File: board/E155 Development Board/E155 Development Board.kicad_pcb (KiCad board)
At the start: 2 copper layers, 106.9 x 105.3 mm, 48 parts, among them J1 Screw_Terminal_01x02, J2 Conn_01x03, J3 Conn_01x02, J4 Conn_01x02, J6 Conn_02x20_Odd_Even, J7 Conn_01x06, SW0 SW_Push, SW1 SW_Push, SW2 SW_Push, SW3 SW_Push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

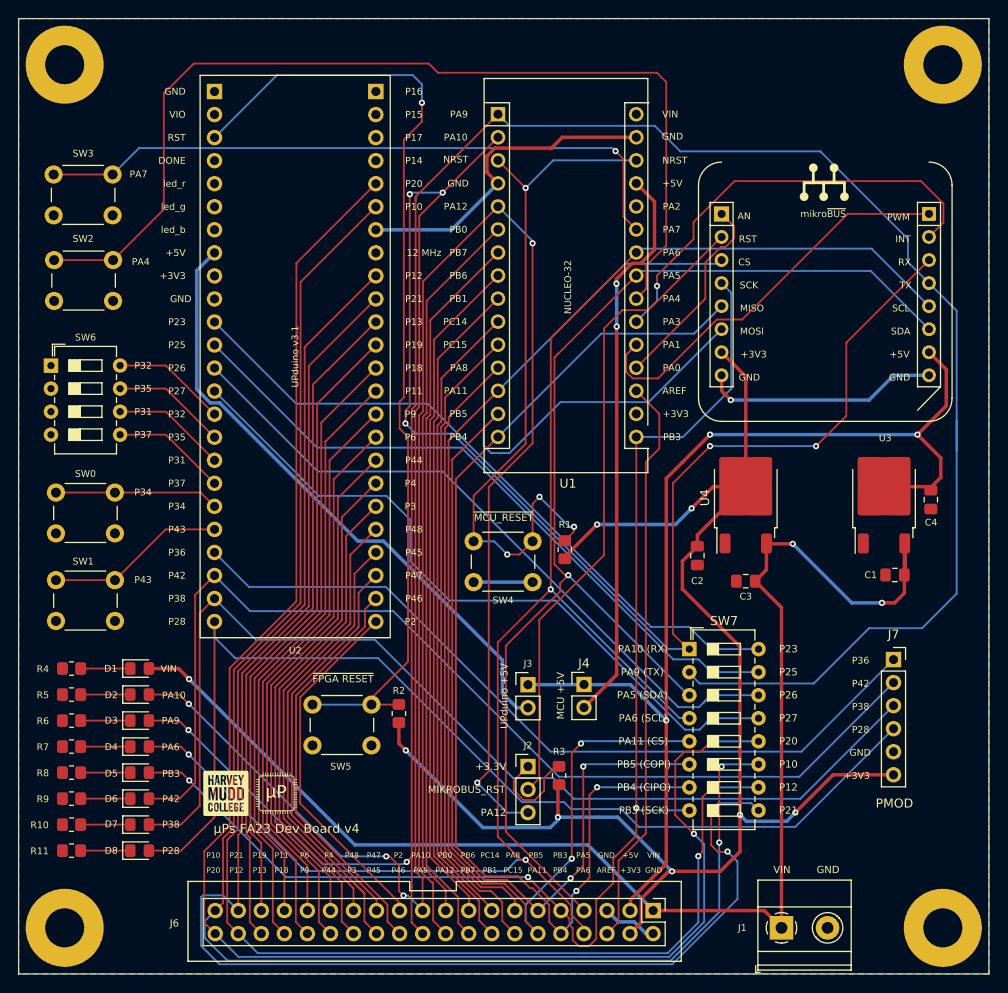
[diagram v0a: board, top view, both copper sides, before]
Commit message: Board updates for FA24
Removed specific text on the board which references a year and changed it to a version number. Also updated the libraries and KiCad files to resolve design check issues.
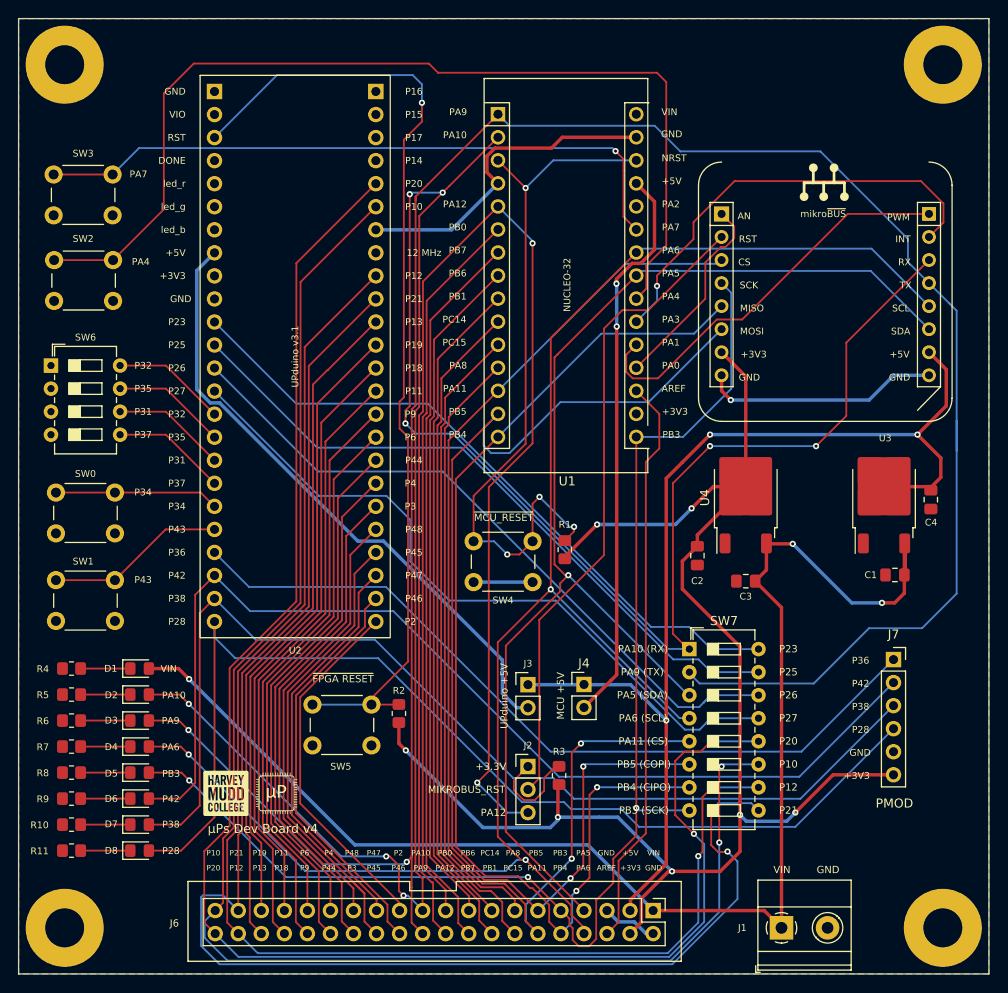
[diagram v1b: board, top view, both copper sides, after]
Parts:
- G***: value LOGO -> MicroPs_LOGO; footprint LOGO -> E155_Footprints:MicroPs_LOGO
- G***: footprint LOGO -> E155_Footprints:LOGO
- moved U1 0.27 mm to (93.2, 104.4)
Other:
- board text added: "µPs Dev Board v4"
- board text removed: "µPs FA23 Dev Board v4"
